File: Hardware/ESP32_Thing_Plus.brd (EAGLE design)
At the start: 22.9 x 50.8 mm, 101 parts, among them J1 AMP FCI 10103594-0001LF, Q1 2.5A/30V, Q2 MBT3904DW1T1, U1 MCP73831, U2 ESP-WROOM-32NARROW, U3 AP2112K-3.3V, U4 CP2102N

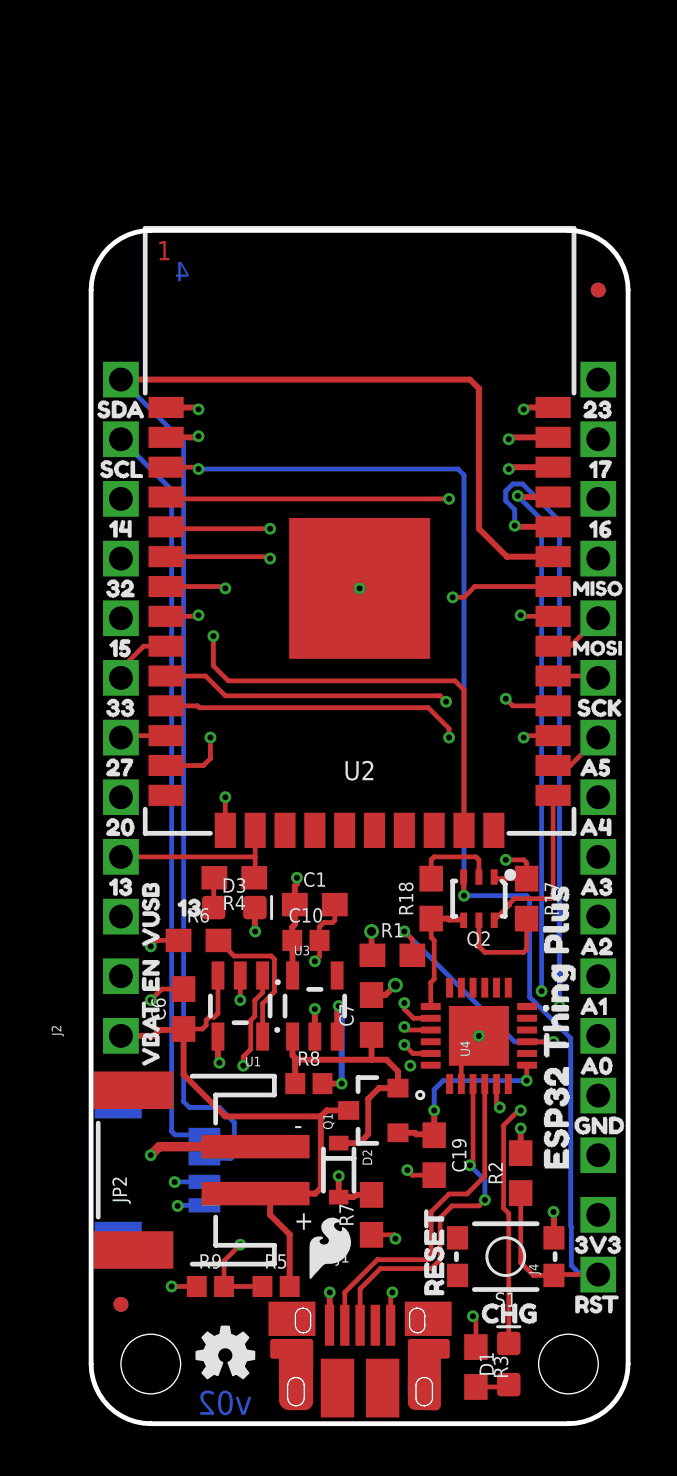
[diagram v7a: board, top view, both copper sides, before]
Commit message: v03 Changes
-Updated size to 2.3x0.9in
- Moved Qwiic connector to top
- Adjusted inner layer copper pour
- Cleaned up traces
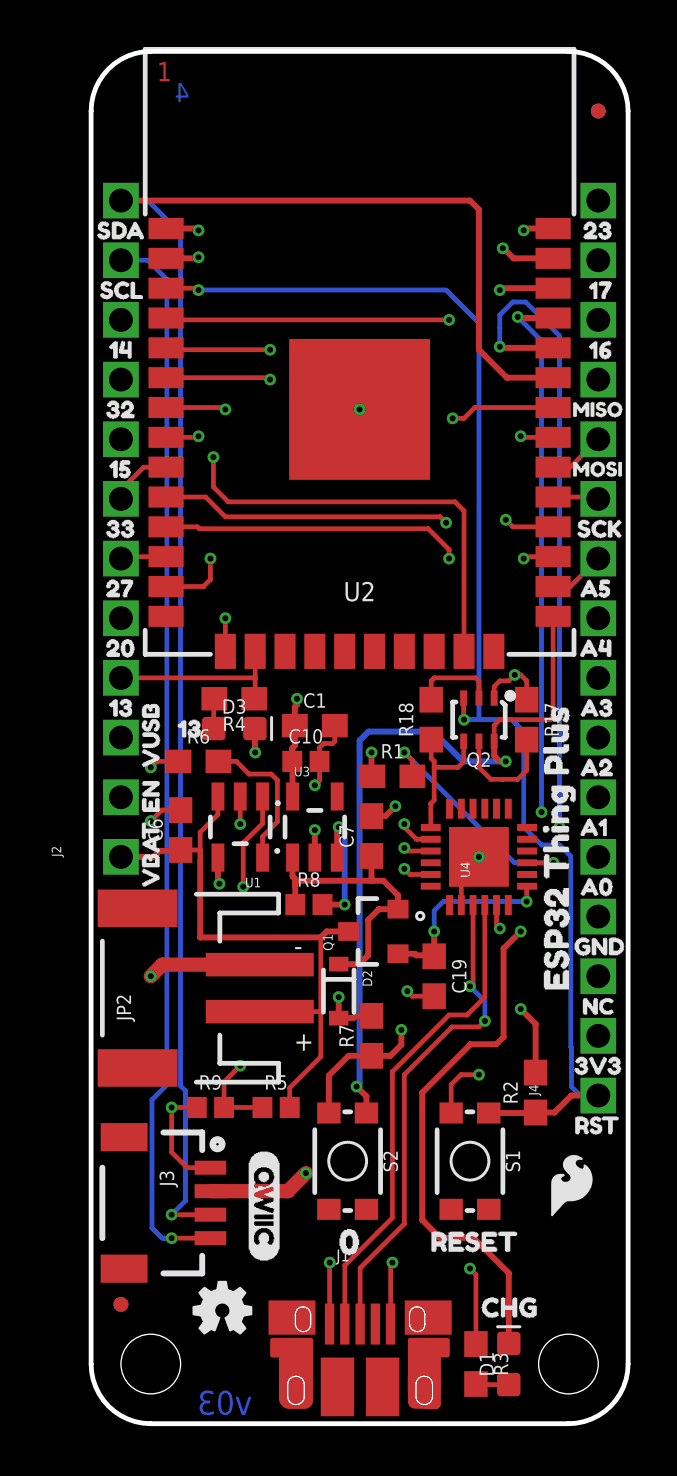
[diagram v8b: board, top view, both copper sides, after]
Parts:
- added S2: 0, SparkFun-Switches:TACTILE_SWITCH_SMD_4.6X2.8MM
- added U$62: (no value), buzzard_labels:00
- added U$63: (no value), buzzard_labels:NC1
- moved LOGO1 10.6 mm to (19.3, 8.51)
- moved JP2 7.75 mm to (3.48, 18.5)
- moved C6 7.62 mm to (3.81, 25.3)
- moved FD1 7.62 mm to (21.6, 55.9)
- moved FD2 7.62 mm to (21.6, 55.9)
- moved U$11 7.62 mm to (5.08, 44.5)
- moved U$21 7.62 mm to (21.2, 44.5)
- moved U$25 7.62 mm to (6.10, 49.5)
- moved U$34 7.62 mm to (0.00, 33.0)
- moved U$4 7.62 mm to (4.83, 47.0)
- moved U$45 7.62 mm to (20.2, 33.0)
- moved U$6 7.62 mm to (21.2, 47.0)
- moved U$61 7.62 mm to (10.2, 47.0)
- moved U$7 7.62 mm to (21.2, 49.5)
- moved U2 7.62 mm to (11.4, 44.5)
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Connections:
- net 0: now also S2.4
- net GND: now also S2.1
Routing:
- net 0: track 7.26 -> 31.8 mm, vias 0 -> 2
- net SCL: track 51.1 -> 64.6 mm, vias 1 -> 2
- net CHG: track 29.5 -> 40.4 mm
- net GND: track 28.7 -> 38.9 mm, vias 19 -> 18
- net SDA: track 62.1 -> 71.9 mm, vias 0 -> 1
- net D+: track 14.7 -> 21.0 mm
- net D-: track 14.5 -> 20.8 mm
- net A4: track 29.8 -> 27.4 mm
- net V_USB: track 15.6 -> 17.7 mm, vias 7 -> 6
- net EN: track 15.3 -> 17.3 mm
- net A3: track 30.4 -> 29.0 mm
- net 35: track 34.9 -> 36.3 mm
- net CHIP_PU: track 58.5 -> 57.2 mm
- net A0: track 28.2 -> 29.4 mm
- net TX: track 35.2 -> 36.1 mm
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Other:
- board size 22.9 x 50.8 mm -> 22.9 x 58.4 mm
- board text added: "Revised by: Alex Wende"
- board text added: "v03"
- board text removed: "v02"
